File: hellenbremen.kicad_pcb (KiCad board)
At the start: 4 copper layers, 102 x 107 mm, 14 parts, among them J3 USB_C_Receptacle_USB2.0_16P, M1 Module-stlink-0.1, M2 Module-power_12and5V-0.2, M3 Module-mega-mcu144-0.6, M4 Module-vr-max9924-0.1, M5 Module-knock-0.2, U1 RNBD451PE-I100

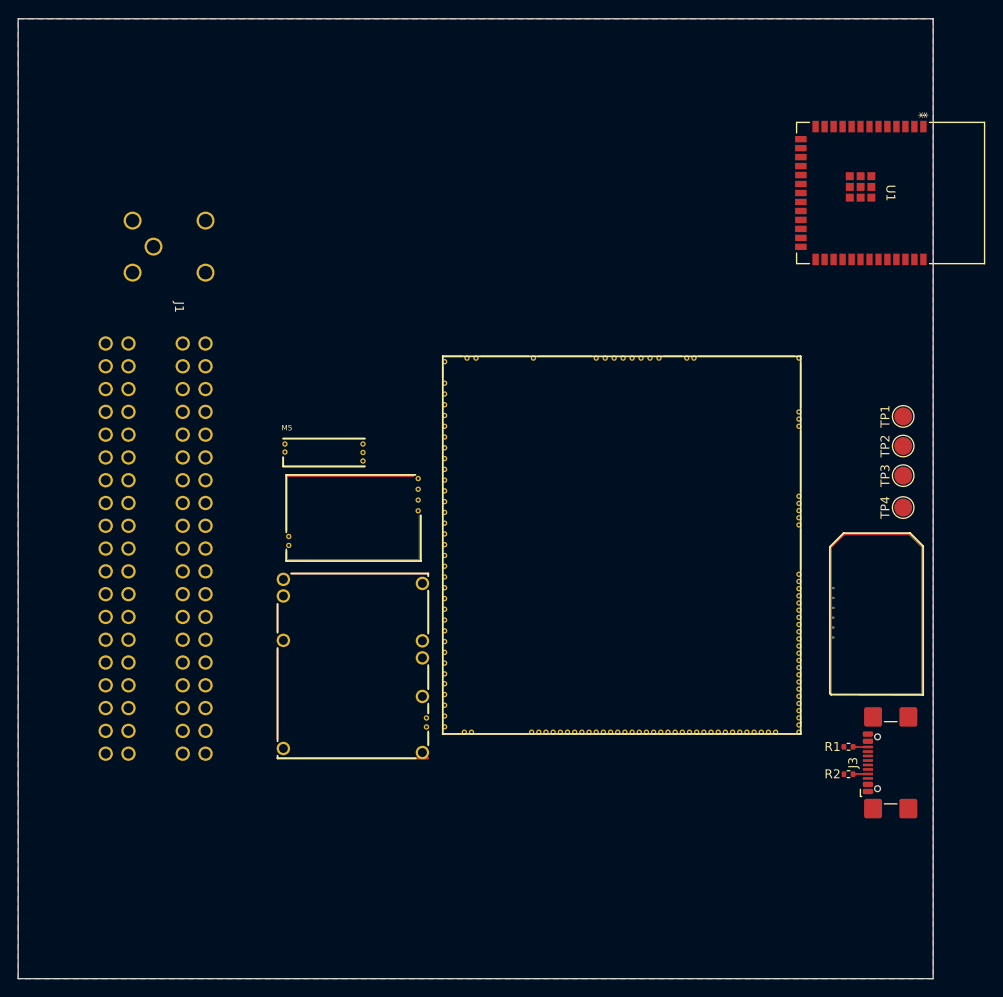
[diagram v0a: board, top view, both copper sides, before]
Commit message: moving origin to bottom left
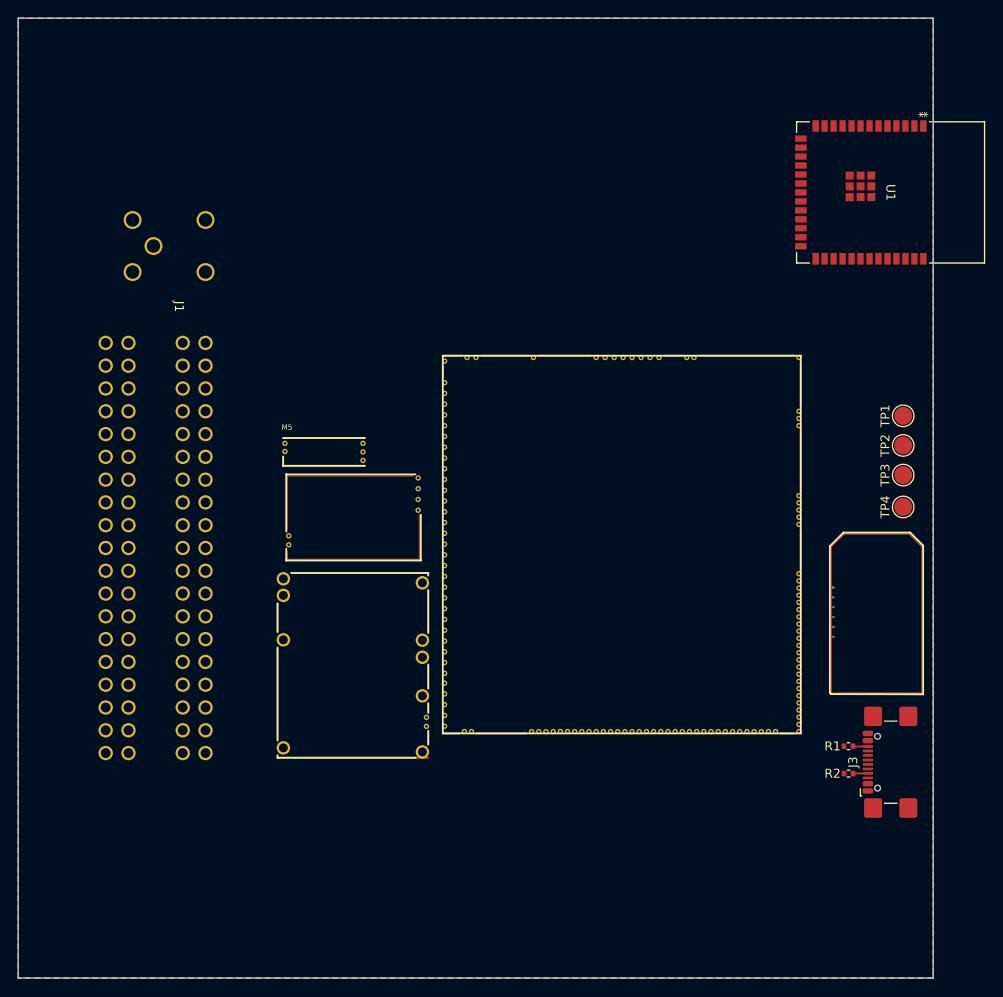
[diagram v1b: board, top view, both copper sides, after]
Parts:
- moved J3 0.07 mm to (159.4, 117.9)
- moved M1 0.07 mm to (151.3, 92.2)
- moved M2 0.07 mm to (89.8, 117.5)
- moved M3 0.07 mm to (108.2, 72.5)
- moved M4 0.07 mm to (90.7, 95.5)
- moved M5 0.07 mm to (90.4, 85.0)
- moved R2 0.07 mm to (153.5, 119.2)
- moved TP1 0.07 mm to (159.6, 79.3)
- moved TP2 0.07 mm to (159.6, 82.6)
- moved TP4 0.07 mm to (159.6, 89.5)
- moved U1 0.07 mm to (158.2, 54.4)
- moved J1 0.07 mm to (73.3, 71.2)
- moved R1 0.07 mm to (153.5, 116.1)
- moved TP3 0.07 mm to (159.6, 85.9)
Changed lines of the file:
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@@
 		(pad_to_mask_clearance 0)
 		(allow_soldermask_bridges_in_footprints no)
-		(aux_axis_origin 60.96 35.052)
-		(grid_origin 60.96 35.052)
+		(aux_axis_origin 60.96 141.986)
+		(grid_origin 60.96 141.986)
 		(pcbplotparams
 			(layerselection 0x00010fc_ffffffff)
@@
 	(footprint "Resistor_SMD:R_0402_1005Metric"
 		(layer "F.Cu")
-		(at 153.522 119.258 180)
+		(at 153.522 119.192 180)
 		(descr "Resistor SMD 0402 (1005 Metric), square (rectangular) end terminal, IPC_7351 nominal, (Body size source: IPC-SM-782 page 72, https://www.pcb-3d.com/wordpress/wp-content/uploads/ipc-sm-782a_amendment_1_and_2.pdf), generated with kicad-footprint-generator")
 		(tags "resistor")
@@
 	(footprint "Resistor_SMD:R_0402_1005Metric"
 		(layer "F.Cu")
-		(at 153.52 116.21 180)
+		(at 153.52 116.144 180)
 		(descr "Resistor SMD 0402 (1005 Metric), square (rectangular) end terminal, IPC_7351 nominal, (Body size source: IPC-SM-782 page 72, https://www.pcb-3d.com/wordpress/wp-content/uploads/ipc-sm-782a_amendment_1_and_2.pdf), generated with kicad-footprint-generator")
 		(tags "resistor")
@@
 	(footprint "0.6:mega-mcu144"
 		(layer "F.Cu")
-		(at 108.195 72.578999 -90)
+		(at 108.195 72.512999 -90)
 		(property "Reference" "M3"
 			(at 43.2181 -40.093895 180)
@@
 			(polygon
 				(pts
-					(xy 108.294999 114.778998) (xy 108.294999 72.678998) (xy 148.194998 72.678998) (xy 148.194998 114.779001)
+					(xy 108.294999 114.712998) (xy 108.294999 72.612998) (xy 148.194998 72.612998) (xy 148.194998 114.713001)
 				)
 			)
@@
 	(footprint "0.1:stlink"
 		(layer "F.Cu")
-		(at 151.342006 92.291003 -90)
+		(at 151.342006 92.225003 -90)
 		(property "Reference" "M1"
 			(at 0.254 -11.3538 -90)
@@
 			(polygon
 				(pts
-					(xy 153.017006 92.516004) (xy 160.317007 92.516004) (xy 161.742006 93.941002) (xy 161.742006 110.291003)
-					(xy 161.717004 110.316004) (xy 151.592006 110.316004) (xy 151.592006 93.991002)
+					(xy 153.017006 92.450004) (xy 160.317007 92.450004) (xy 161.742006 93.875002) (xy 161.742006 110.225003)
+					(xy 161.717004 110.250004) (xy 151.592006 110.250004) (xy 151.592006 93.925002)
 				)
 			)
@@
 			(polygon
 				(pts
-					(xy 152.562994 92.968797) (xy 153.01995 92.511841) (xy 160.323283 92.511841) (xy 160.324909 92.510215)
-					(xy 161.747715 93.933022) (xy 161.747715 110.242054) (xy 161.721698 110.268071) (xy 152.600883 110.268071)
-					(xy 152.600883 110.590994) (xy 151.267012 110.590994) (xy 151.267012 93.865994) (xy 152.31701 92.815996)
-					(xy 152.31701 92.815993)
+					(xy 152.562994 92.902797) (xy 153.01995 92.445841) (xy 160.323283 92.445841) (xy 160.324909 92.444215)
+					(xy 161.747715 93.867022) (xy 161.747715 110.176054) (xy 161.721698 110.202071) (xy 152.600883 110.202071)
+					(xy 152.600883 110.524994) (xy 151.267012 110.524994) (xy 151.267012 93.799994) (xy 152.31701 92.749996)
+					(xy 152.31701 92.749993)
 				)
 			)
@@
 	(footprint "TestPoint:TestPoint_Pad_D2.0mm"
 		(layer "F.Cu")
-		(at 159.616 79.38 90)
+		(at 159.616 79.314 90)
 		(descr "SMD pad as test Point, diameter 2.0mm")
 		(tags "test point SMD pad")
@@
 	(footprint "hellen_knock:knock"
 		(layer "F.Cu")
-		(at 90.398995 85.053003)
+		(at 90.398995 84.987003)
 		(property "Reference" "M5"
 			(at -0.0998 -4.0382 0)
@@
 			(polygon
 				(pts
-					(xy 99.598995 84.953003) (xy 90.498995 84.953003) (xy 90.498995 81.853) (xy 99.598995 81.853)
+					(xy 99.598995 84.887003) (xy 90.498995 84.887003) (xy 90.498995 81.787) (xy 99.598995 81.787)
 				)
 			)
@@
 	(footprint "HD:TE81PINHD"
 		(layer "F.Cu")
-		(at 73.256 71.252 -90)
+		(at 73.256 71.186 -90)
 		(property "Reference" "J1"
 			(at -4.056019 -5.651831 -90)
@@
 	(footprint "TestPoint:TestPoint_Pad_D2.0mm"
 		(layer "F.Cu")
-		(at 159.616 85.984 90)
+		(at 159.616 85.918 90)
 		(descr "SMD pad as test Point, diameter 2.0mm")
 		(tags "test point SMD pad")
@@
 	(footprint "0.2:power_12and5V"
 		(layer "F.Cu")
-		(at 89.772999 117.595001)
+		(at 89.772999 117.529001)
 		(property "Reference" "M2"
 			(at -0.181801 -21.2886 0)
@@
 			(polygon
 				(pts
-					(xy 106.673002 117.495001) (xy 89.872999 117.495001) (xy 89.872999 96.905001) (xy 106.673002 96.905001)
+					(xy 106.673002 117.429001) (xy 89.872999 117.429001) (xy 89.872999 96.839001) (xy 106.673002 96.839001)
 				)
 			)
@@
 	(footprint "footprints:MOD39_15p5X20p7X2p8_ZSX_MCH"
 		(layer "F.Cu")
-		(at 158.21 54.476 -90)
+		(at 158.21 54.41 -90)
 		(tags "RNBD451PE-I100 ")
 		(property "Reference" "U1"
@@
 	(footprint "TestPoint:TestPoint_Pad_D2.0mm"
 		(layer "F.Cu")
-		(at 159.616 89.54 90)
+		(at 159.616 89.474 90)
 		(descr "SMD pad as test Point, diameter 2.0mm")
 		(tags "test point SMD pad")
@@
 	(footprint "TestPoint:TestPoint_Pad_D2.0mm"
 		(layer "F.Cu")
-		(at 159.616 82.682 90)
+		(at 159.616 82.616 90)
 		(descr "SMD pad as test Point, diameter 2.0mm")
 		(tags "test point SMD pad")
@@
 	(footprint "Connector_USB:USB_C_Receptacle_GCT_USB4110"
 		(layer "F.Cu")
-		(at 159.362 117.988 90)
+		(at 159.362 117.922 90)
 		(descr "USB 2.0 Type C Receptacle, GCT, 16P, top mounted, horizontal, 5A, https://gct.co/files/drawings/usb4110.pdf")
 		(tags "USB 2.0 C Type-C Receptacle SMD 16P 16C USB4110-GF-A")
@@
 	(footprint "0.3:vr-max9924"
 		(layer "F.Cu")
-		(at 90.748995 95.601501)
+		(at 90.748995 95.535501)
 		(property "Reference" "M4"
 			(at 2.38 -15.86 0)
@@
 			(polygon
 				(pts
-					(xy 105.748995 95.401501) (xy 90.848995 95.401501) (xy 90.848995 86.001501) (xy 105.748995 86.001501)
+					(xy 105.748995 95.335501) (xy 90.848995 95.335501) (xy 90.848995 85.935501) (xy 105.748995 85.935501)
 				)
 			)
@@
 	)
 	(gr_rect
-		(start 60.96 35.052)
-		(end 162.96 142.052)
+		(start 60.96 34.986)
+		(end 162.96 141.986)
 		(stroke
 			(width 0.05)
@@
 		(layer "Edge.Cuts")
 		(pts
-			(xy 60.96 35.052) (xy 162.96 35.052)
+			(xy 60.96 34.986) (xy 162.96 34.986)
 		)
 		(height -6)
 		(gr_text "102.0000 mm"
-			(at 111.96 27.902 0)
+			(at 111.96 27.836 0)
 			(layer "Edge.Cuts")
 			(effects
@@
 		(layer "Edge.Cuts")
 		(pts
-			(xy 60.96 35.052) (xy 60.96 142.052)
+			(xy 60.96 34.986) (xy 60.96 141.986)
 		)
 		(height 13)
 		(gr_text "107.0000 mm"
-			(at 46.81 88.552 90)
+			(at 46.81 88.486 90)
 			(layer "Edge.Cuts")
 			(effects
@@
 	)
 	(segment
-		(start 154.058 116.238)
-		(end 154.03 116.21)
+		(start 154.058 116.172)
+		(end 154.03 116.144)
 		(width 0.2)
 		(layer "F.Cu")
@@
 	)
 	(segment
-		(start 155.682 116.238)
-		(end 154.058 116.238)
+		(start 155.682 116.172)
+		(end 154.058 116.172)
 		(width 0.2)
 		(layer "F.Cu")
@@
 	)
 	(segment
-		(start 155.682 119.238)
-		(end 154.052 119.238)
+		(start 155.682 119.172)
+		(end 154.052 119.172)
 		(width 0.2)
 		(layer "F.Cu")
@@
 	)
 	(segment
-		(start 154.052 119.238)
-		(end 154.032 119.258)
+		(start 154.052 119.172)
+		(end 154.032 119.192)
 		(width 0.2)
 		(layer "F.Cu")
@@
 		(polygon
 			(pts
-				(xy 60.96 35.052) (xy 162.96 35.052) (xy 162.96 142.052) (xy 60.96 142.052)
+				(xy 60.96 34.986) (xy 162.96 34.986) (xy 162.96 141.986) (xy 60.96 141.986)
 			)
 		)

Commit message: trying to fix aligment
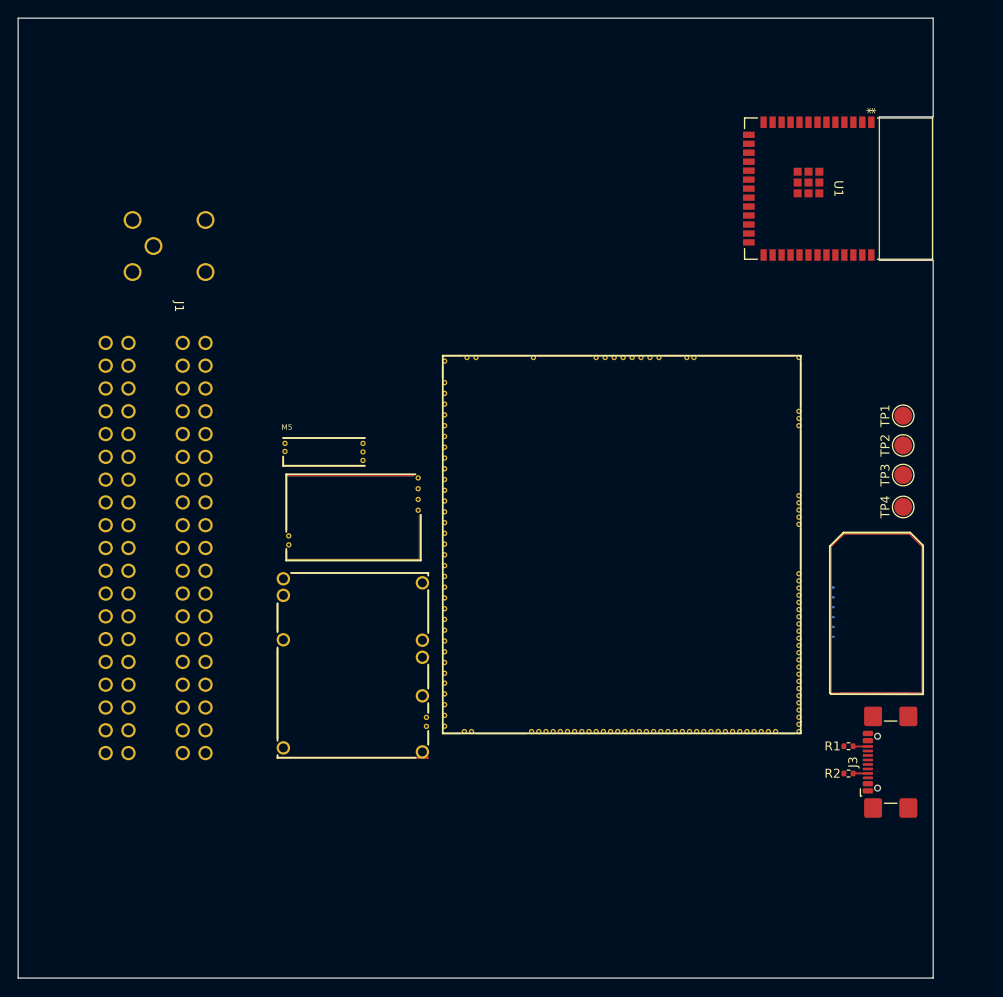
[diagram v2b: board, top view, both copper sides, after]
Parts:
- moved U1 5.82 mm to (152.4, 54.0)
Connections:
- M2 pad E2: unconnected-(M2-V12-PadE2) -> +12V
- M2 pad E3: unconnected-(M2-VIGN-PadE3) -> VIGN
- M2 pad E5: unconnected-(M2-EN_5VP-PadE5) -> PWR_EN
- M3 pad N26: unconnected-(M3-IN_VIGN-PadN26) -> VIGN
- M3 pad N29: unconnected-(M3-OUT_PWR_EN-PadN29) -> PWR_EN
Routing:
- removed copper zone on B.Cu, net GND
- removed copper zone on F.Cu, net GND
- removed copper zone on In1.Cu, net GND
- removed copper zone on In2.Cu, net GND
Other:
- outline, holes or cut-outs redrawn

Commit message: Implementing some inputs and outputs
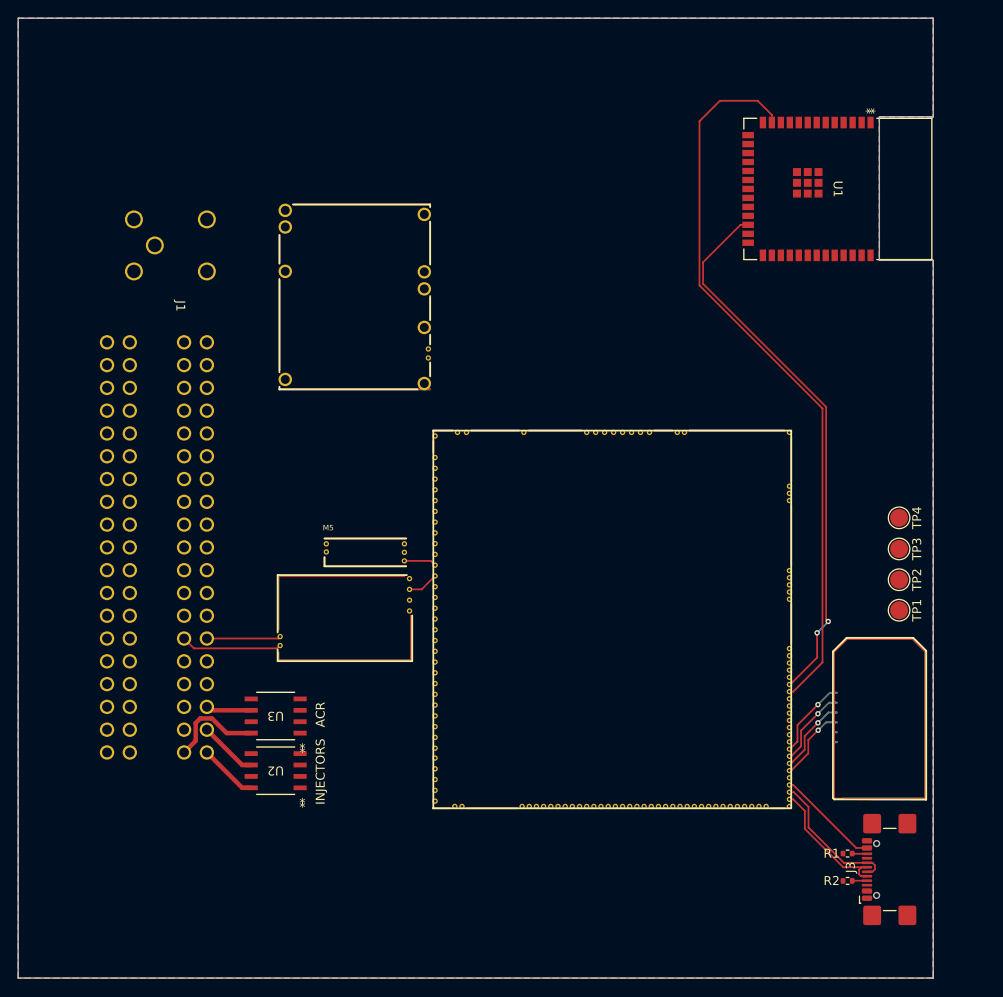
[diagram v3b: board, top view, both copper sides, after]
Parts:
- added U2: VNLD5160TR-E, VNLD5160TR-E:SO_160TR-E_STM, F.Cu at (89.7, 118.9)
- added U3: VNLD5160TR-E, VNLD5160TR-E:SO_160TR-E_STM, F.Cu at (89.7, 112.8)
- moved M2 41.1 mm to (90.0, 76.5)
- moved TP1 21.7 mm to (159.2, 101.0), turned to -90 degrees
- moved TP2 15.0 mm to (159.2, 97.6), turned to -90 degrees
- moved M5 12.1 mm to (95.0, 96.2)
- moved R2 12.0 mm to (153.4, 131.2)
- moved J3 12.0 mm to (159.3, 129.9)
- moved R1 12.0 mm to (153.4, 128.1)
- moved M1 11.7 mm to (151.7, 104.0)
- moved M4 11.3 mm to (89.8, 106.8)
- moved M3 8.42 mm to (107.1, 80.9)
- moved TP3 8.25 mm to (159.2, 94.2), turned to -90 degrees
- moved TP4 1.29 mm to (159.2, 90.7), turned to -90 degrees
- moved J1 0.16 mm to (73.4, 71.1)
- moved U1 0.09 mm to (152.3, 54.0)
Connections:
- J1 pad 11: unconnected-(J1-CKPSL-Pad11) -> CRANK_LOW
- J1 pad 25: unconnected-(J1-FACRE-Pad25) -> ACR_1
- J1 pad 30: unconnected-(J1-CKPSH-Pad30) -> CRANK_HIGH
- J1 pad 5: unconnected-(J1-PSP1-Pad5) -> +12V_PSP
- J1 pad 6: unconnected-(J1-FFI-Pad6) -> INJ_1
- J1 pad 67: unconnected-(J1-BATFU-Pad67) -> +12V_BAT
- J1 pad 7: unconnected-(J1-RFI-Pad7) -> INJ_2
- J1 pad 8: unconnected-(J1-RACRE-Pad8) -> ACR_2
- M2 pad V1: +12V_RAW -> +12V_BAT
- M2 pad V2: unconnected-(M2-IN_VIGN-PadV2) -> +12V_PSP
- M2 pad V3: +12V_RAW -> +12V_PSP
- M3 pad E18: unconnected-(M3-OUT_INJ2-PadE18) -> MCU_INJ2
- M3 pad E19: unconnected-(M3-OUT_INJ1-PadE19) -> MCU_INJ1
- M3 pad E33: unconnected-(M3-OUT_INJ7-PadE33) -> MCU_ACR1
- M3 pad E34: unconnected-(M3-OUT_INJ8-PadE34) -> MCU_ACR2
- M3 pad S32: unconnected-(M3-IN_TPS2-PadS32) -> IN_TPS2
- M3 pad S33: unconnected-(M3-IN_PPS2-PadS33) -> IN_PPS2
- M4 pad G: unconnected-(M4-GND-PadG) -> GND
- M4 pad W1: unconnected-(M4-VR-/HALL-PadW1) -> CRANK_LOW
- M4 pad W2: unconnected-(M4-VR+-PadW2) -> CRANK_HIGH
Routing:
- net UART_BT_TX: track 0.00 -> 81.6 mm
- net UART_BT_RX: track 0.00 -> 61.4 mm, vias 0 -> 2
- net Net-(M3-USBP): track 0.00 -> 15.7 mm
- net Net-(M3-USBM): track 0.00 -> 14.8 mm
- net Net-(M3-VBUS): track 0.00 -> 11.6 mm
- net CRANK_HIGH: track 0.00 -> 11.3 mm
- net ACR_1: track 0.00 -> 10.9 mm
- net Net-(M1-nReset): track 0.00 -> 8.82 mm, vias 0 -> 1
- net Net-(M1-SWCLK): track 0.00 -> 8.65 mm, vias 0 -> 1
- net Net-(M1-SWDIO): track 0.00 -> 8.39 mm, vias 0 -> 1
- net CRANK_LOW: track 0.00 -> 8.25 mm
- net Net-(M1-SWO): track 0.00 -> 8.25 mm, vias 0 -> 1
- net INJ_2: track 0.00 -> 6.57 mm
- net INJ_1: track 0.00 -> 6.57 mm
- net ACR_2: track 0.00 -> 5.10 mm
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- added copper zone on B.Cu, net GND
- added copper zone on F.Cu, net GND
- added copper zone on In1.Cu, net GND
- added copper zone on In2.Cu, net GND
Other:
- board text added: "ACR"
- board text added: "INJECTORS"

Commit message: still initial layout
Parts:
- added C1: 4.7uF 10V, Capacitor_SMD:C_0603_1608Metric, F.Cu at (149.5, 42.5)
- added C2: 0.1uF 10V, Capacitor_SMD:C_0402_1005Metric, F.Cu at (149.5, 45.0)
- added C3: 4.7uF 10V, Capacitor_SMD:C_0603_1608Metric, F.Cu at (144.0, 64.3)
- added C4: 0.1uF 10V, Capacitor_SMD:C_0402_1005Metric, F.Cu at (144.6, 63.0)
- added D1: GREEN, LED_SMD:LED_0402_1005Metric, F.Cu at (145.3, 39.9)
- added D2: BLUE, LED_SMD:LED_0402_1005Metric, F.Cu at (151.4, 45.0)
- added D3: RED, LED_SMD:LED_0402_1005Metric, F.Cu at (153.4, 63.0)
- added J2: Conn_01x03_Pin, Connector_PinHeader_2.54mm:PinHeader_1x03_P2.54mm_Vertical, F.Cu at (151.2, 67.2)
- added R10: 470, Resistor_SMD:R_0402_1005Metric, F.Cu at (155.2, 63.5)
- added R3: 4.7k, Resistor_SMD:R_0402_1005Metric, F.Cu at (100.7, 120.1)
- added R4: 4.7k, Resistor_SMD:R_0402_1005Metric, F.Cu at (100.7, 117.6)
- added R5: 4.7k, Resistor_SMD:R_0402_1005Metric, F.Cu at (100.7, 114.3)
- added R6: 4.7k, Resistor_SMD:R_0402_1005Metric, F.Cu at (100.7, 111.7)
- added R7: 0, Resistor_SMD:R_0402_1005Metric, F.Cu at (149.4, 39.9)
- added R8: 470, Resistor_SMD:R_0402_1005Metric, F.Cu at (147.3, 39.9)
- added R9: 470, Resistor_SMD:R_0402_1005Metric, F.Cu at (151.5, 42.2)
- moved TP4 74.3 mm to (107.1, 37.7)
- moved TP2 14.2 mm to (159.6, 83.4)
- moved TP1 9.72 mm to (159.8, 91.3)
- moved TP3 6.69 mm to (159.8, 87.5)
- moved U2 3.37 mm to (93.0, 118.9)
- moved U3 3.37 mm to (93.0, 112.8)
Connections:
- J1 pad 29: unconnected-(J1-5VSNSGND1-Pad29) -> GND
- J1 pad 74: unconnected-(J1-5VSNSGND2-Pad74) -> GND
- M3 pad N22: unconnected-(M3-V33-PadN22) -> +3V3
- M3 pad N28: unconnected-(M3-V33_SWITCHABLE-PadN28) -> +3V3SW
- M3 pad N32: unconnected-(M3-V33-PadN32) -> +3V3
- U1 pad 27: unconnected-(U1-VDD-Pad27) -> 3V3_VDD_BT
- U1 pad 28: unconnected-(U1-VDD-Pad28) -> 3V3_VDD_BT
- U1 pad 29: unconnected-(U1-PA8-Pad29) -> DEBUG_TX
- U1 pad 31: unconnected-(U1-PA7-Pad31) -> DEBUG_RX
- U1 pad 36: unconnected-(U1-PA3-Pad36) -> Net-(D3-K)
- U1 pad 6: unconnected-(U1-PB5-Pad6) -> Net-(D2-K)
- U1 pad 7: unconnected-(U1-VDD_A-Pad7) -> 3V3_VDD_BT
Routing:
- net CAN_L: track 0.00 -> 61.7 mm, vias 0 -> 2
- net CAN_H: track 0.00 -> 59.8 mm, vias 0 -> 2
- net IN_TPS2: track 0.00 -> 45.4 mm, vias 0 -> 1
- net MCU_INJ2: track 0.00 -> 43.8 mm
- net IN_CLT: track 0.00 -> 42.6 mm
- net IN_IAT: track 0.00 -> 39.7 mm, vias 0 -> 2
- net IN_TPS: track 0.00 -> 37.7 mm
- net IN_MAP: track 0.00 -> 37.6 mm, vias 0 -> 2
- net MCU_INJ1: track 0.00 -> 35.4 mm, vias 0 -> 2
- net MCU_ACR2: track 0.00 -> 34.7 mm
- net MCU_ACR1: track 0.00 -> 34.7 mm
- net IN_PPS2: track 0.00 -> 32.2 mm
- net IN_PPS: track 0.00 -> 32.2 mm
- net +3V3SW: track 0.00 -> 28.5 mm, vias 0 -> 4
- net +12V_PSP: track 0.01 -> 15.4 mm
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- added copper zone on In2.Cu, net +12V
- added copper zone on In2.Cu, net +3V3SW
- added copper zone on In2.Cu, net +5V
- removed copper zone on In2.Cu, net GND
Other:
- board text added: "ACTIVE"
- board text added: "BT DEBUG UART"
- board text added: "BT_POWER"
- board text added: "TXD RXD GND"
